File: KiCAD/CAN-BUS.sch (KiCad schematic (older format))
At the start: 11 parts, among them U13 MCP2551, U14 MCP2515, Y2 16MHz

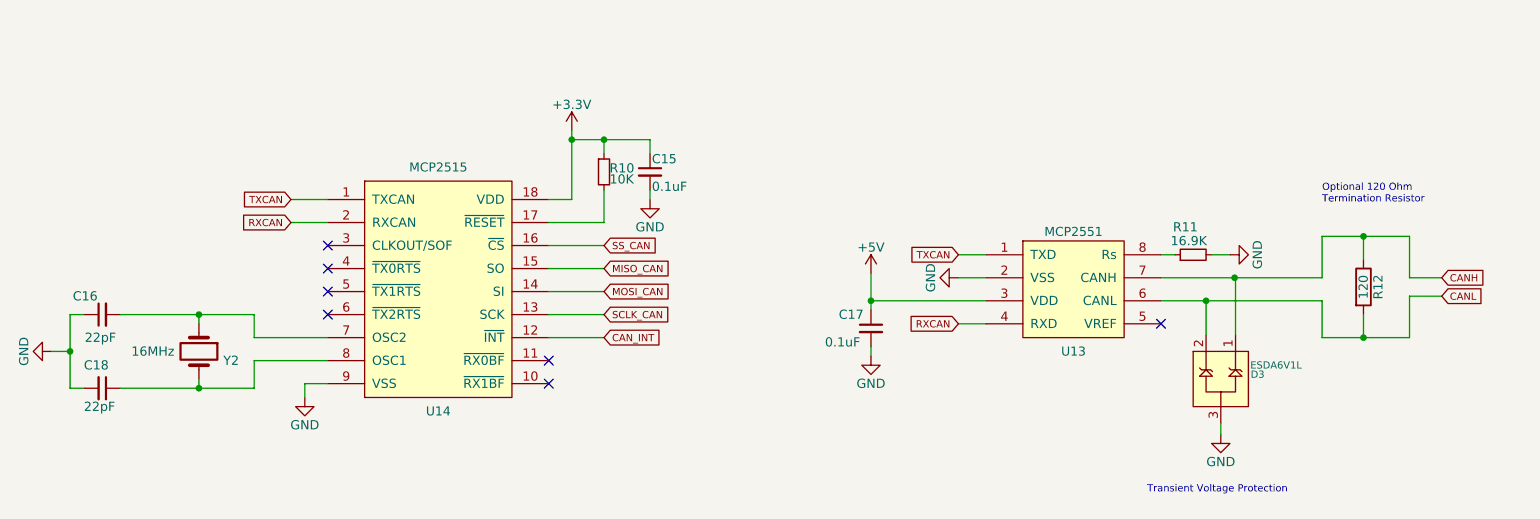
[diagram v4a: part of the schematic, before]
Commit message: Began routing, added differential pair labels
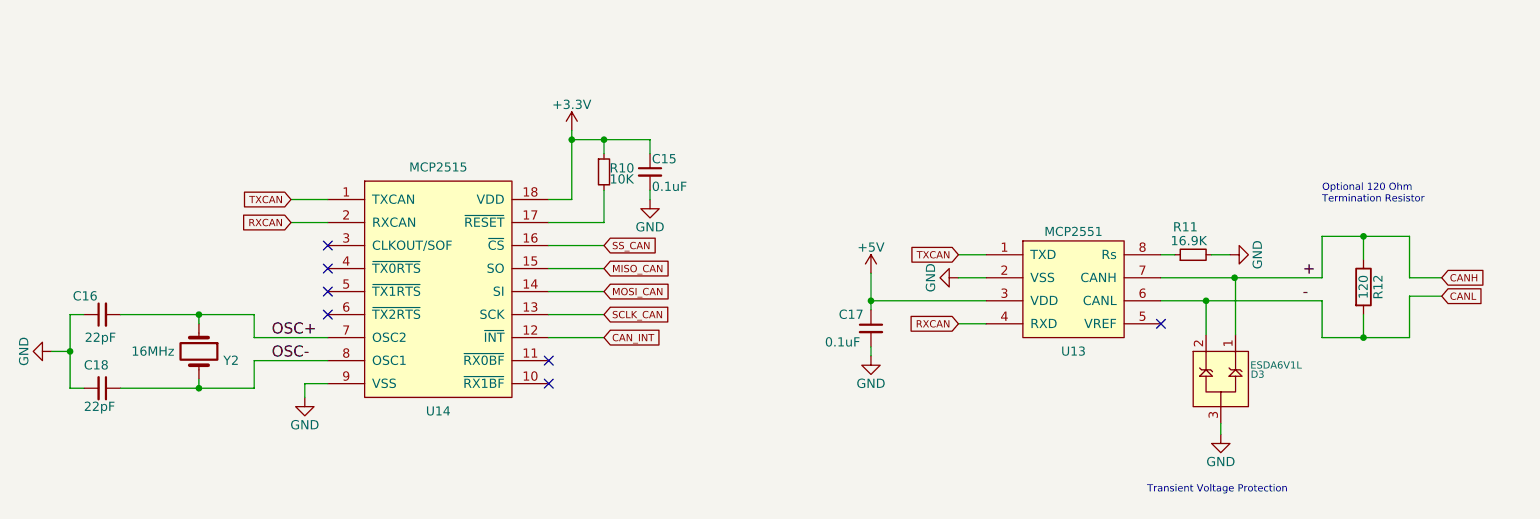
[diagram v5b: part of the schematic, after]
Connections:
- net OSC+: now reaches C16.2, U14.7 (OSC2), Y2.1
- net OSC-: now reaches C18.1, U14.8 (OSC1), Y2.2
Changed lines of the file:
@@
 RXCAN
 $Comp
-L GND #PWR053
+L GND #PWR054
 U 1 1 5C648816
 P 3425 4350
-F 0 "#PWR053" H 3425 4100 50  0001 C CNN
+F 0 "#PWR054" H 3425 4100 50  0001 C CNN
 F 1 "GND" H 3425 4200 50  0000 C CNN
 F 2 "" H 3425 4350 50  0001 C CNN
@@
 	3425 4275 3550 4275
 $Comp
-L +3.3V #PWR054
+L +3.3V #PWR055
 U 1 1 5C6489C6
 P 4875 2900
-F 0 "#PWR054" H 4875 2750 50  0001 C CNN
+F 0 "#PWR055" H 4875 2750 50  0001 C CNN
 F 1 "+3.3V" H 4875 3040 50  0000 C CNN
 F 2 "" H 4875 2900 50  0001 C CNN
@@
 	3150 4025 3150 3900
 Wire Wire Line
-	3150 3900 2850 3900
-Wire Wire Line
-	2850 3900 2425 3900
+	3150 3900 2425 3900
 Wire Wire Line
 	2850 3900 2850 3950
@@
 	2850 4250 2850 4300
 Wire Wire Line
-	2425 4300 2850 4300
-Wire Wire Line
-	2850 4300 3150 4300
+	2425 4300 3150 4300
 Wire Wire Line
 	3150 4300 3150 4150
@@
 $EndComp
 $Comp
-L GND #PWR055
+L GND #PWR056
 U 1 1 5C648CB1
 P 2050 4100
-F 0 "#PWR055" H 2050 3850 50  0001 C CNN
+F 0 "#PWR056" H 2050 3850 50  0001 C CNN
 F 1 "GND" H 2050 3950 50  0000 C CNN
 F 2 "" H 2050 4100 50  0001 C CNN
@@
 	2050 4100 2150 4100
 Wire Wire Line
-	2150 3900 2150 4100
-Wire Wire Line
-	2150 4100 2150 4300
+	2150 3900 2150 4300
 Wire Wire Line
 	2150 3900 2225 3900
@@
 	6975 3575 7125 3575
 $Comp
-L GND #PWR056
+L GND #PWR057
 U 1 1 5C649298
 P 6975 3700
-F 0 "#PWR056" H 6975 3450 50  0001 C CNN
+F 0 "#PWR057" H 6975 3450 50  0001 C CNN
 F 1 "GND" H 6975 3550 50  0000 C CNN
 F 2 "" H 6975 3700 50  0001 C CNN
@@
 	6975 3700 7125 3700
 Wire Wire Line
-	6500 3675 6500 3825
-Wire Wire Line
-	6500 3825 6500 3875
+	6500 3675 6500 3875
 Wire Wire Line
 	6500 3825 7125 3825
@@
 $EndComp
 $Comp
-L GND #PWR057
+L GND #PWR058
 U 1 1 5C649485
 P 8450 3575
-F 0 "#PWR057" H 8450 3325 50  0001 C CNN
+F 0 "#PWR058" H 8450 3325 50  0001 C CNN
 F 1 "GND" H 8450 3425 50  0000 C CNN
 F 2 "" H 8450 3575 50  0001 C CNN
@@
 NoConn ~ 8075 3950
 $Comp
-L GND #PWR058
+L GND #PWR059
 U 1 1 5C649B47
 P 8400 4550
-F 0 "#PWR058" H 8400 4300 50  0001 C CNN
+F 0 "#PWR059" H 8400 4300 50  0001 C CNN
 F 1 "GND" H 8400 4400 50  0000 C CNN
 F 2 "" H 8400 4550 50  0001 C CNN
@@
 	8320 4010 8320 3825
 Wire Wire Line
-	8075 3825 8320 3825
-Wire Wire Line
-	8320 3825 8950 3825
-Wire Wire Line
-	8480 4010 8480 3700
-Wire Wire Line
-	8480 3700 8475 3700
-Wire Wire Line
-	8475 3700 8075 3700
+	8075 3825 8950 3825
+Wire Wire Line
+	8480 3700 8480 4010
+Wire Wire Line
+	8075 3700 8480 3700
 $Comp
 L R R12
@@
 	8950 3700 8950 3475
 Wire Wire Line
-	8950 3475 9175 3475
-Wire Wire Line
-	9175 3475 9425 3475
+	8950 3475 9425 3475
 Wire Wire Line
 	9175 3475 9175 3600
@@
 	9175 3900 9175 4025
 Wire Wire Line
-	8950 4025 9175 4025
-Wire Wire Line
-	9175 4025 9425 4025
+	8950 4025 9425 4025
 Wire Wire Line
 	8950 3825 8950 4025
@@
 $EndComp
 $Comp
-L GND #PWR059
+L GND #PWR060
 U 1 1 5C64ABB3
 P 6500 4125
-F 0 "#PWR059" H 6500 3875 50  0001 C CNN
+F 0 "#PWR060" H 6500 3875 50  0001 C CNN
 F 1 "GND" H 6500 3975 50  0000 C CNN
 F 2 "" H 6500 4125 50  0001 C CNN
@@
 $EndComp
 Wire Wire Line
-	4875 2900 4875 2950
-Wire Wire Line
-	4875 2950 4875 3275
+	4875 2900 4875 3275
 Wire Wire Line
 	4875 3275 4750 3275
 Wire Wire Line
-	4875 2950 5050 2950
-Wire Wire Line
-	5050 2950 5300 2950
+	4875 2950 5300 2950
 Wire Wire Line
 	5050 2950 5050 3025
@@
 Connection ~ 5050 2950
 $Comp
-L GND #PWR060
+L GND #PWR061
 U 1 1 5C64B180
 P 5300 3275
-F 0 "#PWR060" H 5300 3025 50  0001 C CNN
+F 0 "#PWR061" H 5300 3025 50  0001 C CNN
 F 1 "GND" H 5300 3125 50  0000 C CNN
 F 2 "" H 5300 3275 50  0001 C CNN
@@
 $EndComp
 $Comp
-L +5V #PWR?
+L +5V #PWR062
 U 1 1 5C8EBD26
 P 6500 3675
-F 0 "#PWR?" H 6500 3525 50  0001 C CNN
+F 0 "#PWR062" H 6500 3525 50  0001 C CNN
 F 1 "+5V" H 6500 3815 50  0000 C CNN
 F 2 "" H 6500 3675 50  0001 C CNN
@@
 	1    0    0    -1
 $EndComp
+Text Label 3245 4025 0    60   ~ 0
+OSC+
+Text Label 8845 3700 0    60   ~ 0
++
+Text Label 8845 3825 0    60   ~ 0
+-
+Text Label 3245 4150 0    60   ~ 0
+OSC-
 $EndSCHEMATC

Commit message: Redoing layout
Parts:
- added J4: Can Header, Pin_Headers:Pin_Header_Straight_1x02_Pitch2.54mm, symbol Conn_01x02
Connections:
- net CANH renamed +
- net +: now also J4.1 (Pin_1)
- net CANL renamed -
- net -: now also J4.2 (Pin_2)
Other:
- note added: "Pin Headers -> Binder Series 709"
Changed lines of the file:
@@
 	8950 3825 8950 4025
 Connection ~ 8320 3825
-Text GLabel 9600 3700 2    39   Input ~ 0
-CANH
 Wire Wire Line
 	9425 3475 9425 3700
@@
 Wire Wire Line
 	9425 3700 9600 3700
-Text GLabel 9600 3800 2    39   Input ~ 0
-CANL
 Wire Wire Line
 	9600 3800 9425 3800
@@
 Text Label 3245 4150 0    60   ~ 0
 OSC-
+$Comp
+L Conn_01x02 J4
+U 1 1 5C9D17FA
+P 9800 3700
+F 0 "J4" H 9800 3800 50  0000 C CNN
+F 1 "Can Header" H 9800 3500 50  0001 C CNN
+F 2 "Pin_Headers:Pin_Header_Straight_1x02_Pitch2.54mm" H 9800 3700 50  0001 C CNN
+F 3 "" H 9800 3700 50  0001 C CNN
+	1    9800 3700
+	1    0    0    -1
+$EndComp
+Text Notes 9930 3780 0    39   ~ 0
+Pin Headers -> Binder Series 709
 $EndSCHEMATC

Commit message: More Routing
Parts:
- U13: footprint Housings_SOIC:SOIC-8-1EP_3.9x4.9mm_Pitch1.27mm -> Housings_SOIC:SOIC-8_3.9x4.9mm_Pitch1.27mm
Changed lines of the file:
@@
 F 0 "U13" H 7600 3450 49  0000 C CNN
 F 1 "MCP2551" H 7600 4100 49  0000 C CNN
-F 2 "Housings_SOIC:SOIC-8-1EP_3.9x4.9mm_Pitch1.27mm" H 7600 3775 49  0001 C CNN
+F 2 "Housings_SOIC:SOIC-8_3.9x4.9mm_Pitch1.27mm" H 7600 3775 49  0001 C CNN
 F 3 "" H 7600 3775 49  0001 C CNN
 	1    7600 3775

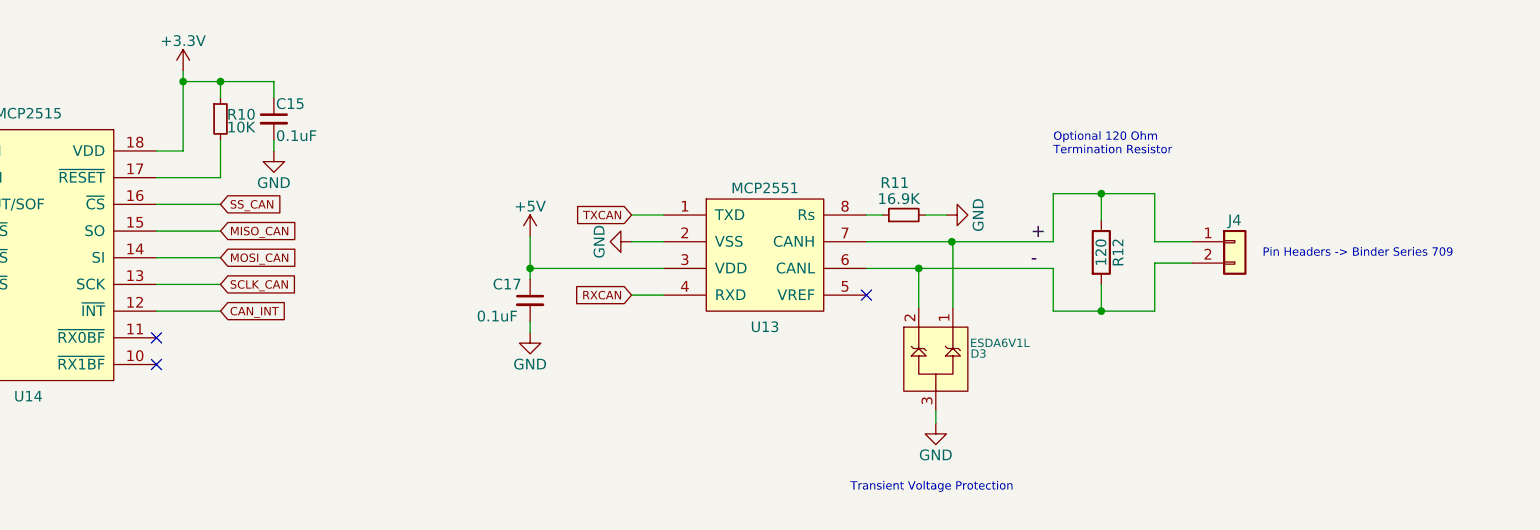
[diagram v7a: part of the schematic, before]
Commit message: Dropped 4 spare sensors, revising layout.
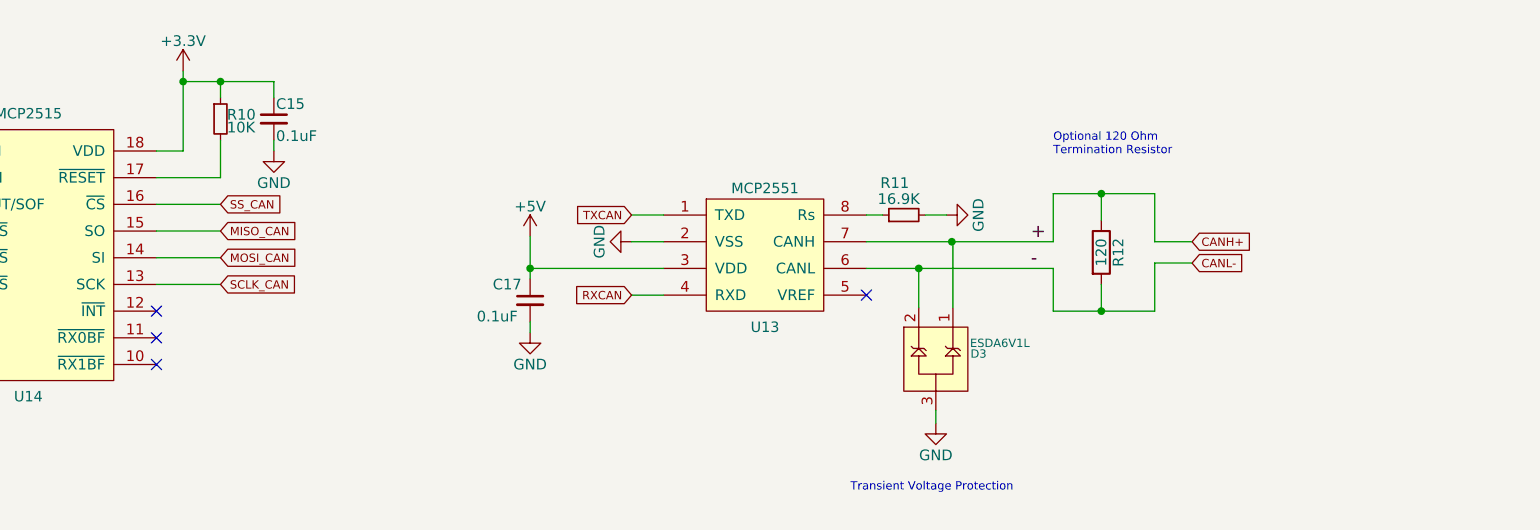
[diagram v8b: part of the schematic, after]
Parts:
- removed J4: Can Header, Pin_Headers:Pin_Header_Straight_1x02_Pitch2.54mm, symbol Conn_01x02
- C15, C17: footprint Capacitors_SMD:C_1206 -> Capacitors_SMD:C_0603
- C16, C18: footprint Capacitors_SMD:C_0805 -> Capacitors_SMD:C_0603
- R10: footprint Resistors_SMD:R_1210 -> Resistors_SMD:R_0603
- R11, R12: footprint Resistors_SMD:R_0805 -> Resistors_SMD:R_0603
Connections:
- net + renamed CANH+
- net - renamed CANL-
- net CAN_INT: no longer names the net of U14.12 (~INT)
- no-connect marks 7 -> 8
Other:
- note removed: "Pin Headers -> Binder Series 709"
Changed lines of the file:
@@
 RXCAN
 $Comp
-L GND #PWR054
+L GND #PWR046
 U 1 1 5C648816
 P 3425 4350
-F 0 "#PWR054" H 3425 4100 50  0001 C CNN
+F 0 "#PWR046" H 3425 4100 50  0001 C CNN
 F 1 "GND" H 3425 4200 50  0000 C CNN
 F 2 "" H 3425 4350 50  0001 C CNN
@@
 	3425 4275 3550 4275
 $Comp
-L +3.3V #PWR055
+L +3.3V #PWR047
 U 1 1 5C6489C6
 P 4875 2900
-F 0 "#PWR055" H 4875 2750 50  0001 C CNN
+F 0 "#PWR047" H 4875 2750 50  0001 C CNN
 F 1 "+3.3V" H 4875 3040 50  0000 C CNN
 F 2 "" H 4875 2900 50  0001 C CNN
@@
 F 0 "R10" H 5080 3145 50  0000 L CNN
 F 1 "10K" H 5080 3085 50  0000 L CNN
-F 2 "Resistors_SMD:R_1210" H 5050 3125 50  0001 C CNN
+F 2 "Resistors_SMD:R_0603" H 5050 3125 50  0001 C CNN
 F 3 "" H 5050 3125 50  0001 C CNN
 	1    5050 3125
@@
 Wire Wire Line
 	5050 3900 4750 3900
-Text GLabel 5050 4025 2    39   Input ~ 0
-CAN_INT
-Wire Wire Line
-	5050 4025 4750 4025
 $Comp
 L Crystal Y2
@@
 F 0 "C16" V 2425 3925 50  0000 L CNN
 F 1 "22pF" V 2200 3825 50  0000 L CNN
-F 2 "Capacitors_SMD:C_0805" H 2325 3900 50  0001 C CNN
+F 2 "Capacitors_SMD:C_0603" H 2325 3900 50  0001 C CNN
 F 3 "" H 2325 3900 50  0001 C CNN
 	1    2325 3900
@@
 F 0 "C18" V 2200 4200 50  0000 L CNN
 F 1 "22pF" V 2425 4200 50  0000 L CNN
-F 2 "Capacitors_SMD:C_0805" H 2325 4300 50  0001 C CNN
+F 2 "Capacitors_SMD:C_0603" H 2325 4300 50  0001 C CNN
 F 3 "" H 2325 4300 50  0001 C CNN
 	1    2325 4300
@@
 $EndComp
 $Comp
-L GND #PWR056
+L GND #PWR048
 U 1 1 5C648CB1
 P 2050 4100
-F 0 "#PWR056" H 2050 3850 50  0001 C CNN
+F 0 "#PWR048" H 2050 3850 50  0001 C CNN
 F 1 "GND" H 2050 3950 50  0000 C CNN
 F 2 "" H 2050 4100 50  0001 C CNN
@@
 	6975 3575 7125 3575
 $Comp
-L GND #PWR057
+L GND #PWR049
 U 1 1 5C649298
 P 6975 3700
-F 0 "#PWR057" H 6975 3450 50  0001 C CNN
+F 0 "#PWR049" H 6975 3450 50  0001 C CNN
 F 1 "GND" H 6975 3550 50  0000 C CNN
 F 2 "" H 6975 3700 50  0001 C CNN
@@
 F 0 "R11" V 8400 3550 50  0000 L CNN
 F 1 "16.9K" V 8325 3500 50  0000 L CNN
-F 2 "Resistors_SMD:R_0805" H 8250 3575 50  0001 C CNN
+F 2 "Resistors_SMD:R_0603" H 8250 3575 50  0001 C CNN
 F 3 "" H 8250 3575 50  0001 C CNN
 	1    8250 3575
@@
 $EndComp
 $Comp
-L GND #PWR058
+L GND #PWR050
 U 1 1 5C649485
 P 8450 3575
-F 0 "#PWR058" H 8450 3325 50  0001 C CNN
+F 0 "#PWR050" H 8450 3325 50  0001 C CNN
 F 1 "GND" H 8450 3425 50  0000 C CNN
 F 2 "" H 8450 3575 50  0001 C CNN
@@
 NoConn ~ 8075 3950
 $Comp
-L GND #PWR059
+L GND #PWR051
 U 1 1 5C649B47
 P 8400 4550
-F 0 "#PWR059" H 8400 4300 50  0001 C CNN
+F 0 "#PWR051" H 8400 4300 50  0001 C CNN
 F 1 "GND" H 8400 4400 50  0000 C CNN
 F 2 "" H 8400 4550 50  0001 C CNN
@@
 F 0 "R12" V 9255 3750 50  0000 C CNN
 F 1 "120" V 9175 3750 50  0000 C CNN
-F 2 "Resistors_SMD:R_0805" V 9105 3750 50  0001 C CNN
+F 2 "Resistors_SMD:R_0603" V 9105 3750 50  0001 C CNN
 F 3 "" H 9175 3750 50  0001 C CNN
 	1    9175 3750
@@
 F 0 "C17" H 6325 4050 50  0000 L CNN
 F 1 "0.1uF" H 6250 3900 50  0000 L CNN
-F 2 "Capacitors_SMD:C_1206" H 6500 3975 50  0001 C CNN
+F 2 "Capacitors_SMD:C_0603" H 6500 3975 50  0001 C CNN
 F 3 "" H 6500 3975 50  0001 C CNN
 	1    6500 3975
@@
 $EndComp
 $Comp
-L GND #PWR060
+L GND #PWR052
 U 1 1 5C64ABB3
 P 6500 4125
-F 0 "#PWR060" H 6500 3875 50  0001 C CNN
+F 0 "#PWR052" H 6500 3875 50  0001 C CNN
 F 1 "GND" H 6500 3975 50  0000 C CNN
 F 2 "" H 6500 4125 50  0001 C CNN
@@
 F 0 "C15" H 5310 3195 50  0000 L CNN
 F 1 "0.1uF" H 5310 3045 50  0000 L CNN
-F 2 "Capacitors_SMD:C_1206" H 5300 3125 50  0001 C CNN
+F 2 "Capacitors_SMD:C_0603" H 5300 3125 50  0001 C CNN
 F 3 "" H 5300 3125 50  0001 C CNN
 	1    5300 3125
@@
 Connection ~ 5050 2950
 $Comp
-L GND #PWR061
+L GND #PWR053
 U 1 1 5C64B180
 P 5300 3275
-F 0 "#PWR061" H 5300 3025 50  0001 C CNN
+F 0 "#PWR053" H 5300 3025 50  0001 C CNN
 F 1 "GND" H 5300 3125 50  0000 C CNN
 F 2 "" H 5300 3275 50  0001 C CNN
@@
 $EndComp
 $Comp
-L +5V #PWR062
+L +5V #PWR054
 U 1 1 5C8EBD26
 P 6500 3675
-F 0 "#PWR062" H 6500 3525 50  0001 C CNN
+F 0 "#PWR054" H 6500 3525 50  0001 C CNN
 F 1 "+5V" H 6500 3815 50  0000 C CNN
 F 2 "" H 6500 3675 50  0001 C CNN
@@
 Text Label 3245 4150 0    60   ~ 0
 OSC-
-$Comp
-L Conn_01x02 J4
-U 1 1 5C9D17FA
-P 9800 3700
-F 0 "J4" H 9800 3800 50  0000 C CNN
-F 1 "Can Header" H 9800 3500 50  0001 C CNN
-F 2 "Pin_Headers:Pin_Header_Straight_1x02_Pitch2.54mm" H 9800 3700 50  0001 C CNN
-F 3 "" H 9800 3700 50  0001 C CNN
-	1    9800 3700
-	1    0    0    -1
-$EndComp
-Text Notes 9930 3780 0    39   ~ 0
-Pin Headers -> Binder Series 709
+Text GLabel 9600 3700 2    39   Input ~ 0
+CANH+
+Text GLabel 9600 3800 2    39   Input ~ 0
+CANL-
+NoConn ~ 4750 4025
 $EndSCHEMATC
